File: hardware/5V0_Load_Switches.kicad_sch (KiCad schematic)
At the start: 29 parts, among them Q18 SI2302DDS-T1-GE3, Q19 SI2302DDS-T1-GE3, Q20 SI2302DDS-T1-GE3, U1 LMV321RIYLT, U2 INA199C1DCKR, U3 INA199C1DCKR, U4 INA199C1DCKR, U5 NVTFS5116PLTAG, U6 NVTFS5116PLTAG, U7 NVTFS5116PLTAG

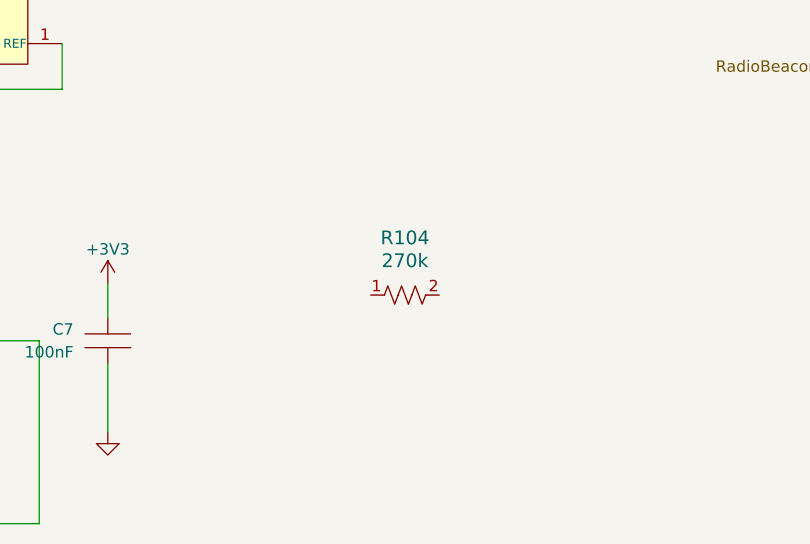
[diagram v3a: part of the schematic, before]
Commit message: hardware: update on footprints
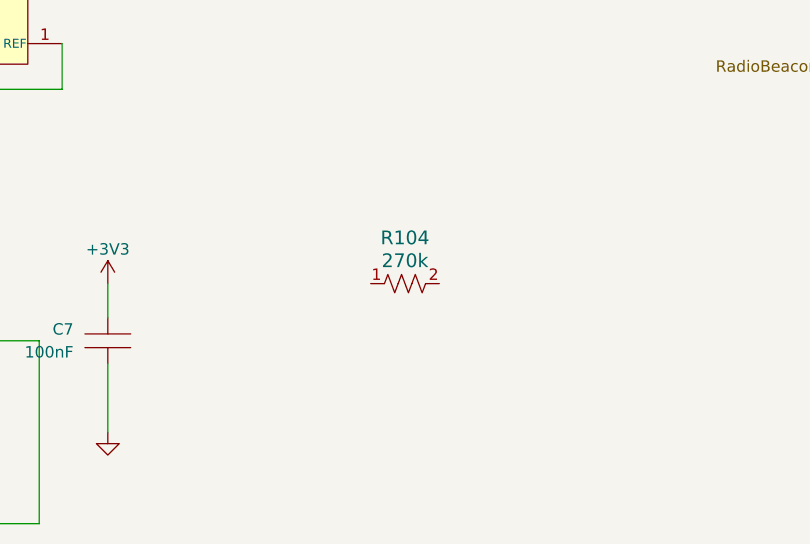
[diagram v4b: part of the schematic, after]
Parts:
- R104: footprint RES_CRCW_0805_VIS -> footprints:CRCW0805270KFKEAHP; symbol CRCW0805270KFKEAHP:CRCW080520K0FKEAHP -> CRCW0805270KFKEAHP:CRCW0805270KFKEAHP
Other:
- moved on the sheet: R104
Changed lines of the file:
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@@
     )
   )
-  (symbol (lib_id "CRCW0805270KFKEAHP:CRCW080520K0FKEAHP") (at 107.95 163.83 0) (unit 1)
+  (symbol (lib_id "CRCW0805270KFKEAHP:CRCW0805270KFKEAHP") (at 107.95 163.83 0) (unit 1)
     (in_bom yes) (on_board yes) (dnp no)
     (property "Reference" "R104" (at 114.3 158.75 0)
@@
       (effects (font (size 1.524 1.524)))
     )
-    (property "Footprint" "RES_CRCW_0805_VIS" (at 107.95 163.83 0)
+    (property "Footprint" "footprints:CRCW0805270KFKEAHP" (at 114.3 166.37 0)
       (effects (font (size 1.27 1.27) italic) hide)
     )
-    (property "Datasheet" "CRCW0805270KFKEAHP" (at 107.95 163.83 0)
+    (property "Datasheet" "CRCW080520K0FKEAHP" (at 113.03 168.91 0)
       (effects (font (size 1.27 1.27) italic) hide)
     )

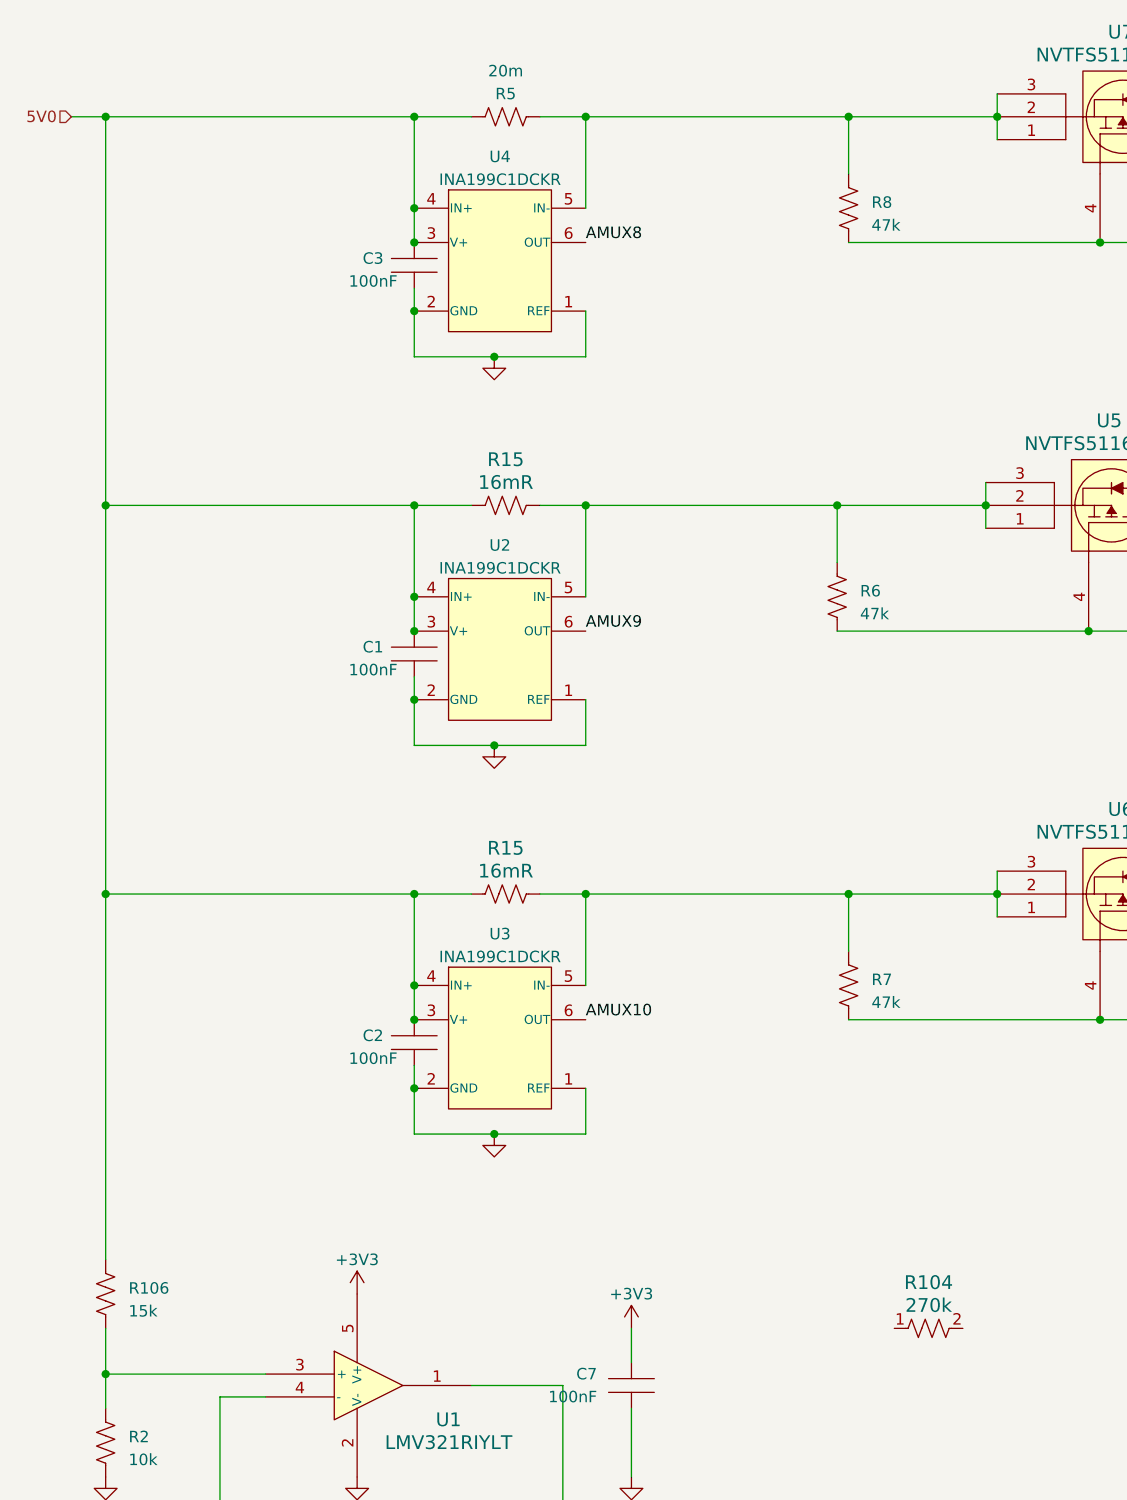
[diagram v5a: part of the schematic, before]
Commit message: hardware: Updating some footprints and 3D models.
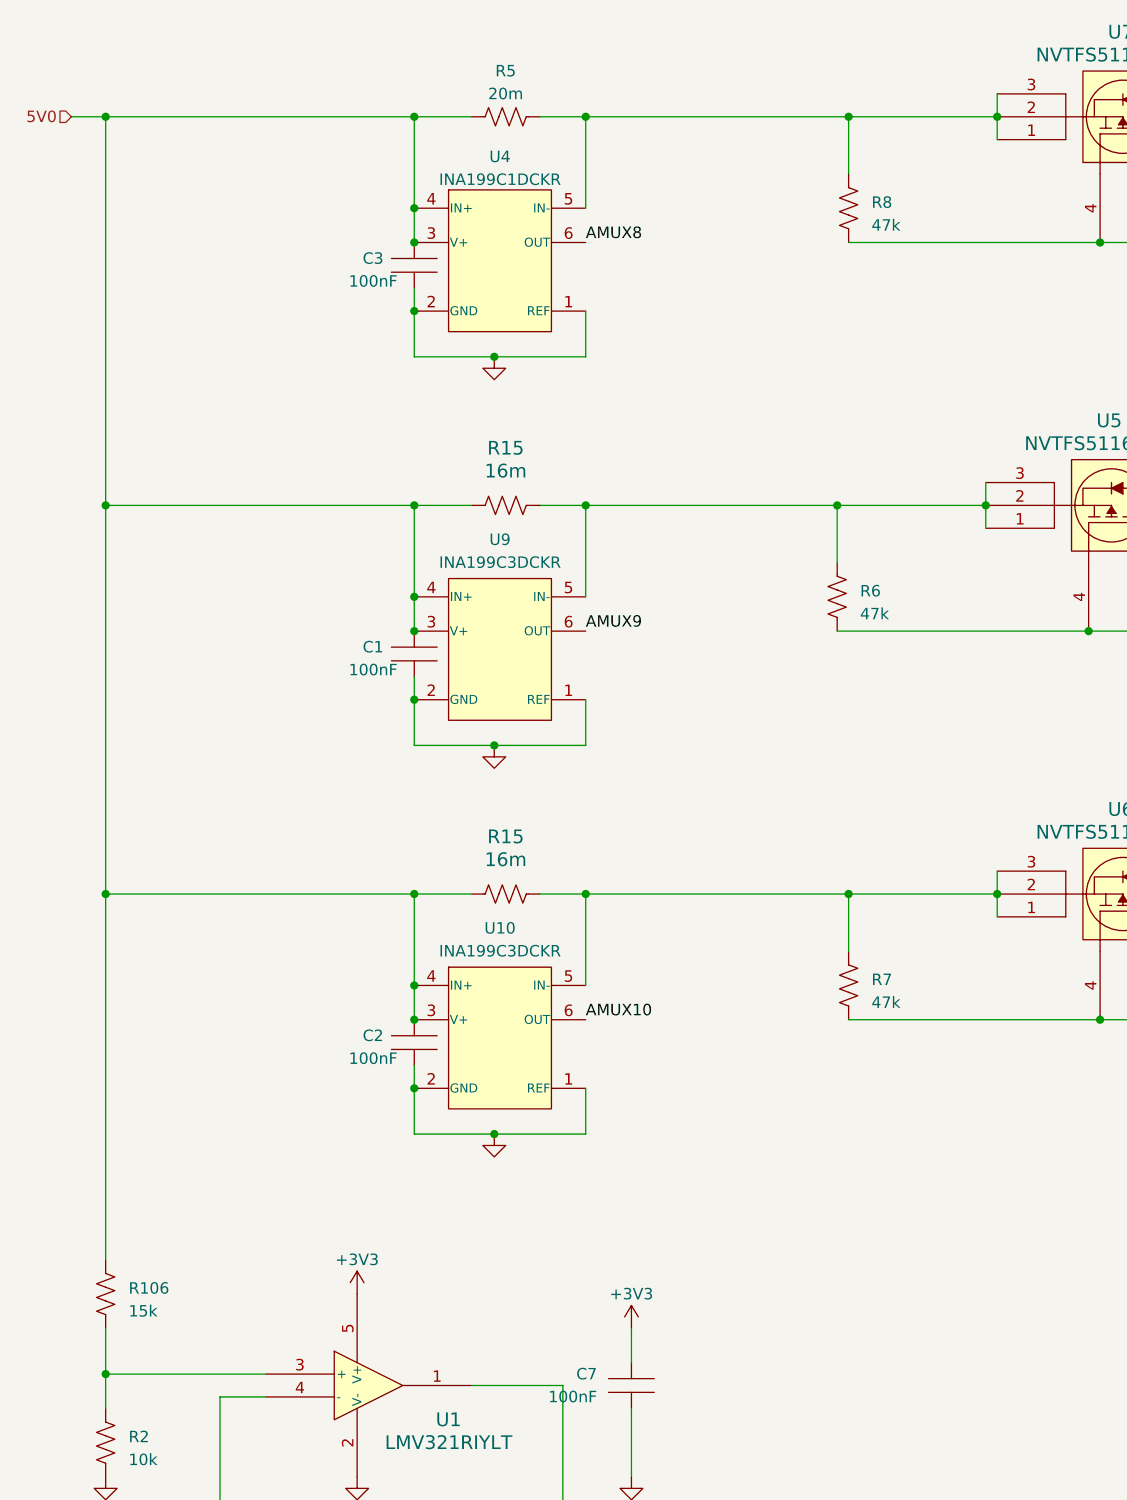
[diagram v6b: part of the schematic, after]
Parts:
- removed R104: 270k, footprints:CRCW0805270KFKEAHP, symbol CRCW0805270KFKEAHP:CRCW0805270KFKEAHP
- removed U2, U3: INA199C1DCKR, footprints:INA199C1DCKR, symbol INA199C1DCKR:INA199xxDCK
- added U10, U9: INA199C3DCKR, Package_TO_SOT_SMD:SOT-363_SC-70-6, symbol INA199C3DCKR:INA199xxDCK
- R15: value 16mR -> 16m
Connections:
- net +5V: now also U10.3 (V+), U10.4 (IN+), U9.3 (V+), U9.4 (IN+)
- net AMUX10: now also U10.6 (OUT)
- net AMUX9: now also U9.6 (OUT)
- net GND: now also U10.1 (REF), U10.2 (GND), U9.1 (REF), U9.2 (GND)
- net at R15.2, R7.2, U6.1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: now also U10.5 (IN-)
- net at R15.2, R6.2, U5.1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: now also U9.5 (IN-)

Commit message: hardware: Updating 3D models, component placement and more.
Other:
- title: (none) -> Reliability Enhanced Electrical Power System
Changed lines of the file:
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@@
 (kicad_sch (version 20230121) (generator eeschema)
   (paper "A4")
+  (title_block
+    (title "Reliability Enhanced Electrical Power System")
+    (date "2023-08-03")
+    (rev "v0.0")
+    (comment 1 "João C. E. Barcellos <joaoclaudiobarcellos@gmail.com>")
+    (comment 2 "Laura Debastiani <laudebastiani@gmail.com>")
+  )
   (junction (at 57.15 43.18) (diameter 0) (color 0 0 0 0)
   )
